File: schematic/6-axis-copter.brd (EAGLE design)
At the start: 70 x 70 mm, 96 parts, among them SW1 SS12D01G4

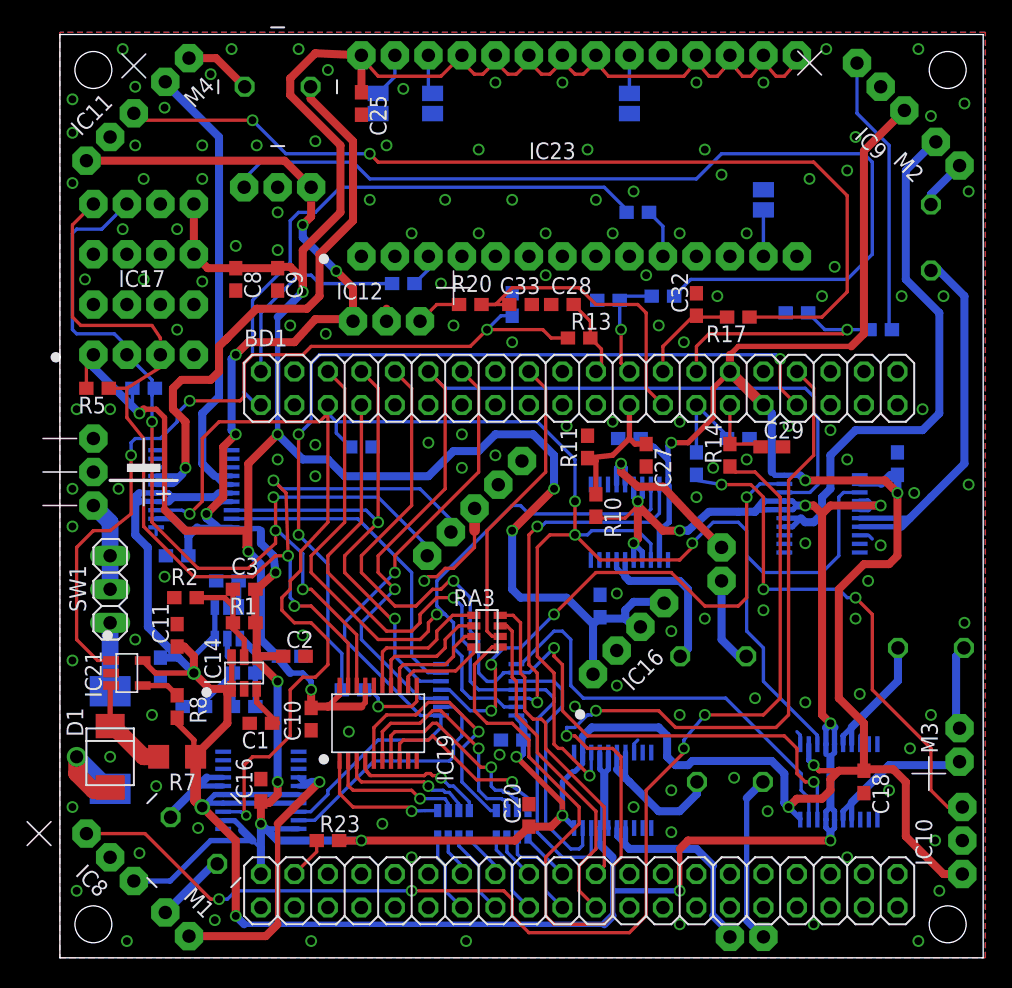
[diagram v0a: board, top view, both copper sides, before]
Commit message: 基板製造メーカー(P板.com)の指摘を元にPCBボード図を修正
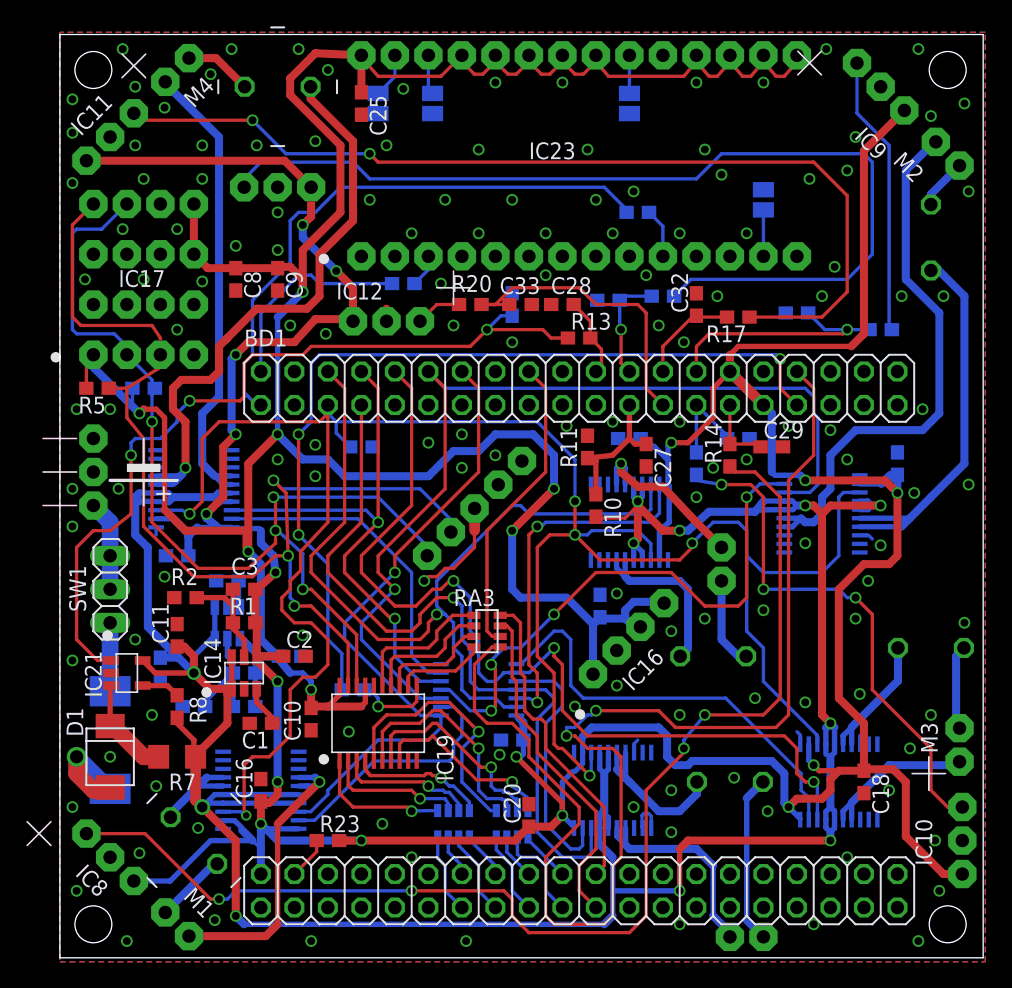
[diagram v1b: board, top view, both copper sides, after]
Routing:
- net GND: track 14.2 -> 17.0 mm
- net BAT: track 224.0 -> 224.9 mm
- net N$2: track 22.0 -> 22.6 mm
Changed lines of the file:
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@@
 <setting verticaltext="up"/>
 </settings>
-<grid distance="0.00625" unitdist="inch" unit="mm" style="lines" multiple="1" display="yes" altdistance="0.025" altunitdist="inch" altunit="inch"/>
+<grid distance="0.00625" unitdist="inch" unit="inch" style="lines" multiple="1" display="yes" altdistance="0.025" altunitdist="inch" altunit="inch"/>
 <layers>
-<layer number="1" name="Top" color="4" fill="1" visible="yes" active="yes"/>
+<layer number="1" name="Top" color="4" fill="1" visible="no" active="yes"/>
 <layer number="16" name="Bottom" color="1" fill="1" visible="yes" active="yes"/>
 <layer number="17" name="Pads" color="2" fill="1" visible="yes" active="yes"/>
@@
 <layer number="19" name="Unrouted" color="6" fill="1" visible="yes" active="yes"/>
 <layer number="20" name="Dimension" color="15" fill="1" visible="yes" active="yes"/>
-<layer number="21" name="tPlace" color="7" fill="1" visible="yes" active="yes"/>
+<layer number="21" name="tPlace" color="7" fill="1" visible="no" active="yes"/>
 <layer number="22" name="bPlace" color="7" fill="1" visible="yes" active="yes"/>
-<layer number="23" name="tOrigins" color="15" fill="1" visible="yes" active="yes"/>
+<layer number="23" name="tOrigins" color="15" fill="1" visible="no" active="yes"/>
 <layer number="24" name="bOrigins" color="15" fill="1" visible="yes" active="yes"/>
-<layer number="25" name="tNames" color="7" fill="1" visible="yes" active="yes"/>
+<layer number="25" name="tNames" color="7" fill="1" visible="no" active="yes"/>
 <layer number="26" name="bNames" color="7" fill="1" visible="yes" active="yes"/>
 <layer number="27" name="tValues" color="7" fill="1" visible="no" active="yes"/>
@@
 <layer number="37" name="tTest" color="7" fill="1" visible="no" active="yes"/>
 <layer number="38" name="bTest" color="7" fill="1" visible="no" active="yes"/>
-<layer number="39" name="tKeepout" color="4" fill="11" visible="yes" active="yes"/>
+<layer number="39" name="tKeepout" color="4" fill="11" visible="no" active="yes"/>
 <layer number="40" name="bKeepout" color="1" fill="11" visible="yes" active="yes"/>
-<layer number="41" name="tRestrict" color="4" fill="10" visible="yes" active="yes"/>
+<layer number="41" name="tRestrict" color="4" fill="10" visible="no" active="yes"/>
 <layer number="42" name="bRestrict" color="1" fill="10" visible="yes" active="yes"/>
-<layer number="43" name="vRestrict" color="2" fill="10" visible="yes" active="yes"/>
+<layer number="43" name="vRestrict" color="2" fill="10" visible="no" active="yes"/>
 <layer number="44" name="Drills" color="7" fill="1" visible="no" active="yes"/>
 <layer number="45" name="Holes" color="7" fill="1" visible="no" active="yes"/>
@@
 <hole x="67.31" y="2.54" drill="2.8"/>
 <hole x="67.31" y="67.31" drill="2.8"/>
+<wire x1="60.96" y1="16.51" x2="60.96" y2="16.03375" width="0.254" layer="42"/>
+<wire x1="61.595" y1="16.35125" x2="61.595" y2="16.1925" width="0.254" layer="42"/>
+<wire x1="61.595" y1="10.4775" x2="61.595" y2="10.63625" width="0.254" layer="42"/>
+<wire x1="43.815" y1="15.39875" x2="43.815" y2="15.5575" width="0.254" layer="42"/>
+<wire x1="44.45" y1="15.71625" x2="44.45" y2="15.5575" width="0.254" layer="42"/>
+<wire x1="43.815" y1="9.8425" x2="43.815" y2="10.00125" width="0.254" layer="42"/>
+<wire x1="44.45" y1="9.68375" x2="44.45" y2="9.525" width="0.254" layer="42"/>
+<wire x1="12.54125" y1="15.24" x2="12.3825" y2="15.24" width="0.254" layer="42"/>
+<wire x1="18.0975" y1="15.24" x2="17.93875" y2="15.24" width="0.254" layer="42"/>
+<wire x1="7.46125" y1="37.465" x2="7.3025" y2="37.465" width="0.254" layer="42"/>
+<wire x1="7.3025" y1="38.1" x2="7.46125" y2="38.1" width="0.254" layer="42"/>
+<wire x1="13.17625" y1="38.1" x2="13.0175" y2="38.1" width="0.254" layer="42"/>
+<wire x1="41.275" y1="35.8775" x2="41.275" y2="35.71875" width="0.254" layer="42"/>
+<wire x1="40.64" y1="36.03625" x2="40.64" y2="35.8775" width="0.254" layer="42"/>
+<wire x1="40.64" y1="30.32125" x2="40.64" y2="30.1625" width="0.254" layer="42"/>
+<wire x1="55.08625" y1="31.75" x2="54.9275" y2="31.75" width="0.254" layer="42"/>
+<wire x1="55.08625" y1="31.115" x2="54.9275" y2="31.115" width="0.254" layer="42"/>
+<wire x1="60.48375" y1="31.75" x2="60.6425" y2="31.75" width="0.254" layer="42"/>
+<wire x1="60.48375" y1="31.115" x2="60.6425" y2="31.115" width="0.254" layer="42"/>
 </plain>
 <attributes>
@@
 <wire x1="9.788025" y1="1.641971875" x2="15.611971875" y2="1.641971875" width="0.6096" layer="1"/>
 <wire x1="15.611971875" y1="1.641971875" x2="16.51" y2="2.54" width="0.6096" layer="1"/>
-<wire x1="16.51" y1="2.54" x2="16.51" y2="8.89" width="0.4064" layer="1"/>
-<wire x1="16.51" y1="8.89" x2="16.51" y2="10.16" width="0.4064" layer="1"/>
+<wire x1="16.51" y1="2.54" x2="16.51" y2="10.16" width="0.4064" layer="1"/>
 <wire x1="16.51" y1="10.16" x2="19.685" y2="13.335" width="0.6096" layer="1"/>
 <via x="19.685" y="13.335" extent="1-16" drill="0.6"/>
-<wire x1="19.685" y1="13.335" x2="19.05" y2="13.335" width="0.6096" layer="16"/>
-<wire x1="19.05" y1="13.335" x2="18.44" y2="13.335" width="0.4064" layer="16"/>
-<wire x1="18.44" y1="13.335" x2="18.1" y2="13.675" width="0.4064" layer="16"/>
 <wire x1="18.1" y1="13.025" x2="18.74" y2="13.025" width="0.4064" layer="16"/>
-<wire x1="18.74" y1="13.025" x2="19.05" y2="13.335" width="0.254" layer="16"/>
+<wire x1="18.1" y1="13.675" x2="19.345" y2="13.675" width="0.4064" layer="16"/>
+<wire x1="19.345" y1="13.675" x2="19.685" y2="13.335" width="0.6096" layer="16"/>
+<wire x1="18.74" y1="13.025" x2="19.375" y2="13.025" width="0.4064" layer="16"/>
+<wire x1="19.375" y1="13.025" x2="19.685" y2="13.335" width="0.6096" layer="16"/>
 </signal>
 <signal name="MOTER-PWM-P-1">
@@
 <wire x1="56.13" y1="16.895" x2="55.88" y2="17.145" width="0.254" layer="16"/>
 <wire x1="24.765" y1="48.26" x2="24.765" y2="49.2125" width="0.6096" layer="1"/>
-<polygon width="0.254" layer="16" isolate="0.254" orphans="yes">
-<vertex x="0" y="70.1675"/>
-<vertex x="0" y="0"/>
-<vertex x="70.1675" y="0"/>
-<vertex x="70.1675" y="70.1675"/>
-</polygon>
-<polygon width="0.254" layer="1" isolate="0.254" orphans="yes">
-<vertex x="0" y="70.1675"/>
-<vertex x="0" y="0"/>
-<vertex x="70.1675" y="0"/>
-<vertex x="70.1675" y="70.1675"/>
-</polygon>
 <via x="4.7625" y="68.8975" extent="1-16" drill="0.6"/>
 <via x="0.9525" y="65.0875" extent="1-16" drill="0.6"/>
@@
 <via x="18.415" y="24.4475" extent="1-16" drill="0.6"/>
 <via x="62.23" y="31.27375" extent="1-16" drill="0.6"/>
+<polygon width="0.254" layer="16" isolate="0.254">
+<vertex x="0" y="70.1675"/>
+<vertex x="0" y="-0.3175"/>
+<vertex x="70.1675" y="-0.3175"/>
+<vertex x="70.1675" y="70.1675"/>
+</polygon>
+<polygon width="0.254" layer="1" isolate="0.254">
+<vertex x="0" y="70.1675"/>
+<vertex x="0" y="-0.3175"/>
+<vertex x="70.1675" y="-0.3175"/>
+<vertex x="70.1675" y="70.1675"/>
+</polygon>
+<wire x1="44.835" y1="9.84" x2="44.835" y2="10.7275" width="0.254" layer="16"/>
+<wire x1="44.835" y1="10.7275" x2="44.60875" y2="10.95375" width="0.254" layer="16"/>
+<wire x1="44.60875" y1="10.95375" x2="44.29125" y2="10.95375" width="0.254" layer="16"/>
+<wire x1="44.29125" y1="10.95375" x2="44.1325" y2="10.795" width="0.254" layer="16"/>
+<wire x1="44.1325" y1="10.795" x2="44.1325" y2="9.8925" width="0.254" layer="16"/>
+<wire x1="44.1325" y1="9.8925" x2="44.185" y2="9.84" width="0.254" layer="16"/>
 </signal>
 <signal name="DISTANCE-1">
@@
 <wire x1="40.935" y1="15.56" x2="40.935" y2="14.31" width="0.4064" layer="16"/>
 <wire x1="40.935" y1="14.31" x2="41.275" y2="13.97" width="0.4064" layer="16"/>
-<wire x1="41.275" y1="13.97" x2="41.275" y2="10.15" width="0.6096" layer="16"/>
-<wire x1="41.275" y1="10.15" x2="41.585" y2="9.84" width="0.4064" layer="16"/>
-<wire x1="41.275" y1="10.15" x2="41.245" y2="10.15" width="0.254" layer="16"/>
-<wire x1="41.245" y1="10.15" x2="40.935" y2="9.84" width="0.4064" layer="16"/>
 <wire x1="41.585" y1="15.56" x2="41.585" y2="14.28" width="0.4064" layer="16"/>
 <wire x1="41.585" y1="14.28" x2="41.275" y2="13.97" width="0.4064" layer="16"/>
@@
 <wire x1="55.245" y1="33.9725" x2="52.86375" y2="33.9725" width="0.4064" layer="16"/>
 <wire x1="52.86375" y1="33.9725" x2="52.705" y2="33.81375" width="0.254" layer="16"/>
+<wire x1="40.935" y1="9.84" x2="40.935" y2="10.7725" width="0.4064" layer="16"/>
+<wire x1="40.935" y1="10.7725" x2="41.195625" y2="11.033125" width="0.6096" layer="16"/>
+<wire x1="41.195625" y1="11.033125" x2="41.275" y2="11.1125" width="0.6096" layer="16"/>
+<wire x1="41.275" y1="11.1125" x2="41.275" y2="13.97" width="0.6096" layer="16"/>
+<wire x1="41.585" y1="9.84" x2="41.585" y2="10.64375" width="0.4064" layer="16"/>
+<wire x1="41.585" y1="10.64375" x2="41.195625" y2="11.033125" width="0.4064" layer="16"/>
 </signal>
 <signal name="4.5V">
@@
 </signal>
 </signals>
+<errors>
+</errors>
 </board>
 </drawing>
